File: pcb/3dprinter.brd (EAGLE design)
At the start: 100 x 80 mm, 79 parts, among them IC1 NRF51822, Q1 MOSFET, Q2 MOSFET, Q3 MOSFET, Q4 MOSFET, Y1 CRYSTAL

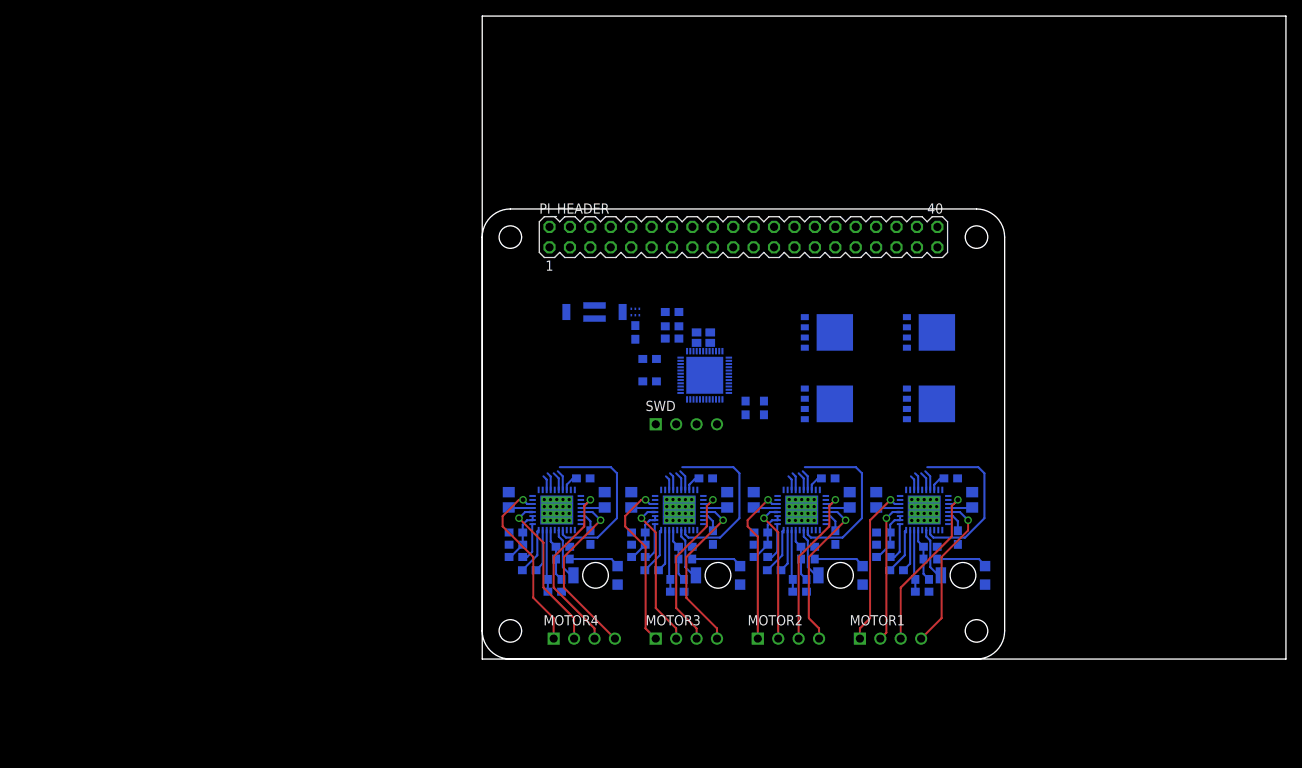
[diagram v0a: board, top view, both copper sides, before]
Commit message: Added regulator and fan mosfet
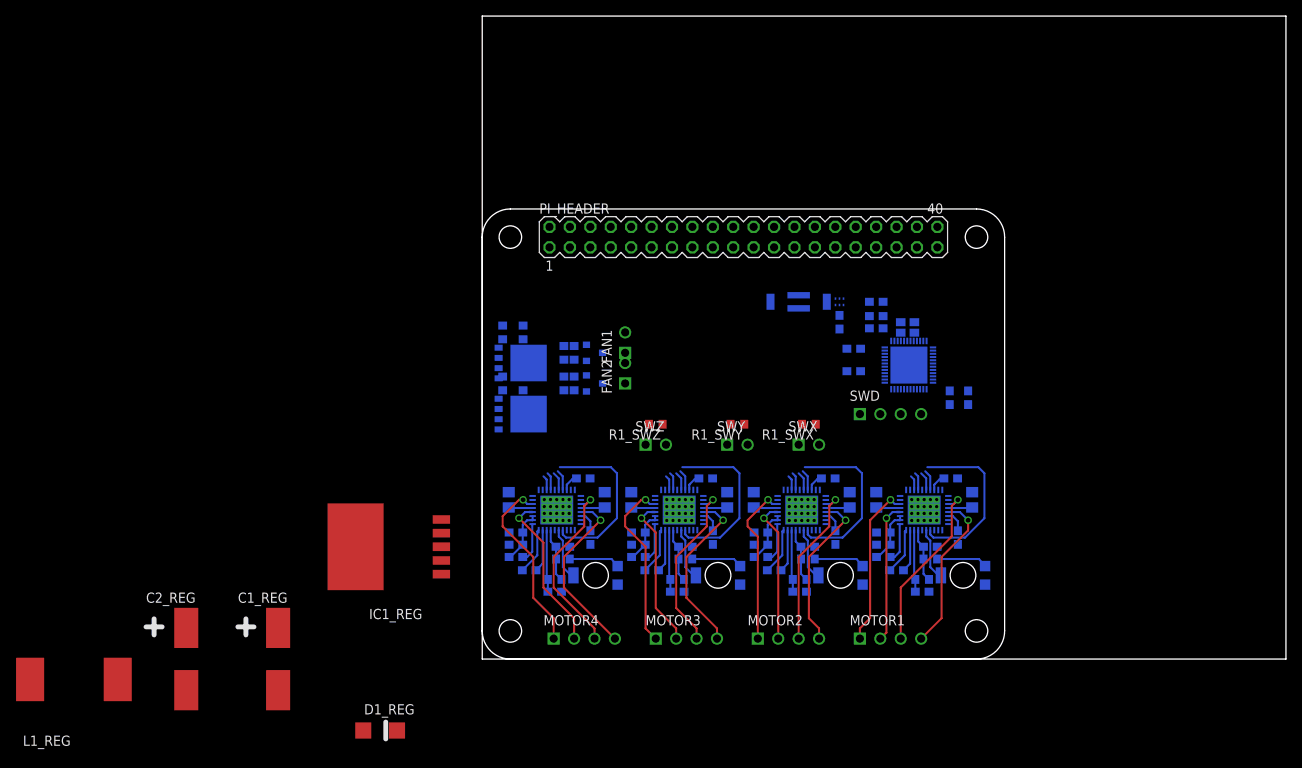
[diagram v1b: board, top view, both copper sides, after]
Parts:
- removed Q1, Q2, Q3, Q4: MOSFET, 3dprinter:MOSFET
- added C1_REG: 560u, 3dprinter:TANTULUM
- added C2_REG: 390u, 3dprinter:TANTULUM
- added D1_REG: SCHOTTKY, 3dprinter:SCHOTTKY
- added FAN1, FAN2, SWX, SWY, SWZ: (no value), 3dprinter:MA02-1
- added IC1_REG: REGULATOR, 3dprinter:REGULATOR
- added L1_REG: 33u, 3dprinter:INDUCTOR
- added Q1_BED, Q1_NOZ: MOSFET, 3dprinter:MOSFET
- added Q1_FAN1, Q1_FAN2: MOSFETSOT23, 3dprinter:SOT23
- added R1_BED, R1_FAN1, R1_FAN2, R1_NOZ: 100R, 3dprinter:R0603
- added R1_SWX, R1_SWY, R1_SWZ: 10k, 3dprinter:R0603
- added R2_BED, R2_FAN1, R2_FAN2, R2_NOZ: 100k, 3dprinter:R0603
- moved BAL 25.4 mm to (44.5, 44.5)
- moved C1 25.4 mm to (44.5, 41.9)
- moved C10 25.4 mm to (46.2, 35.8)
- moved C15 25.4 mm to (46.2, 38.6)
- moved Y1 25.4 mm to (52.9, 41.3)
- moved ANT 25.4 mm to (39.4, 44.5)
- moved C11 25.4 mm to (49.0, 41.1)
- moved C12 25.4 mm to (49.0, 44.5)
- moved C13 25.4 mm to (58.2, 32.5)
- moved C14 25.4 mm to (60.5, 32.5)
- moved C9 25.4 mm to (49.0, 42.7)
- moved IC1 25.4 mm to (53.1, 36.6)
- moved SWD 25.4 mm to (50.8, 30.5)
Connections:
- new net BED: R1_BED.1
- new net BEDG: Q1_BED.4, R1_BED.2, R2_BED.2
- new net FAN1: R1_FAN1.1
- new net FAN1-: FAN1.1, Q1_FAN1.3
- new net FAN1G: Q1_FAN1.1, R1_FAN1.2, R2_FAN1.2
- new net FAN2: R1_FAN2.1
- new net FAN2-: FAN2.1, Q1_FAN2.3
- new net FAN2G: Q1_FAN2.1, R1_FAN2.2, R2_FAN2.2
- new net N$11: Q1_NOZ.TAB
- new net N$12: Q1_BED.TAB
- new net N$13: D1_REG.C, IC1_REG.2, L1_REG.1
- new net NOZ: R1_NOZ.1
- new net NOZG: Q1_NOZ.4, R1_NOZ.2, R2_NOZ.2
- new net SWX: R1_SWX.1, SWX.2
- new net SWY: R1_SWY.1, SWY.2
- new net SWZ: R1_SWZ.1, SWZ.2
- net +12V: now also C1_REG.+, FAN1.2, FAN2.2, IC1_REG.1
- net +3V3: now also R1_SWX.2, R1_SWY.2, R1_SWZ.2
- net +5V: now also C2_REG.+, IC1_REG.4, L1_REG.2
- net GND: now also C1_REG.-, C2_REG.-, D1_REG.A, IC1_REG.3, IC1_REG.5, IC1_REG.TAB, Q1_BED.1, Q1_BED.2, Q1_BED.3, Q1_FAN1.2, Q1_FAN2.2, Q1_NOZ.1, Q1_NOZ.2, Q1_NOZ.3, R2_BED.1, R2_FAN1.1, R2_FAN2.1, R2_NOZ.1, SWX.1, SWY.1, SWZ.1

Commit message: Started component placment
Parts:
- added +12V: (no value), 3dprinter:MA04-1_5MM
- added BED, NOZ: (no value), 3dprinter:MA04-1
- added C3_REG: 1u, 3dprinter:C0805
- added C4_REG: 10n, 3dprinter:C0603
- added C5_REG: 2.2u, 3dprinter:C0805
- added IC2_REG: LP2985-3V3, 3dprinter:SOT23
- Q1_FAN1, Q1_FAN2: device 3dprinter:SOT23 -> 3dprinter:SOT23_FAN
- moved L1_REG 110.0 mm to (40.3, 59.1), flipped to the bottom, turned to 90 degrees
- moved C2_REG 97.4 mm to (37.0, 63.5)
- moved D1_REG 91.8 mm to (43.7, 63.6), flipped to the bottom
- moved C1_REG 89.4 mm to (37.5, 63.5), turned to 180 degrees
- moved IC1_REG 67.1 mm to (39.0, 64.5), flipped to the bottom
- moved R1_FAN1 49.2 mm to (48.0, 71.0), turned to 0 degrees
- moved R2_FAN1 43.8 mm to (36.0, 73.5), turned to 180 degrees
- moved Q1_FAN1 42.5 mm to (39.0, 72.5), turned to 180 degrees
- moved Q1_FAN2 40.1 mm to (29.0, 71.5), turned to 180 degrees
- moved R1_FAN2 37.5 mm to (25.5, 69.0), turned to 0 degrees
- moved R2_FAN2 34.7 mm to (23.0, 66.5), turned to 180 degrees
- moved FAN1 31.9 mm to (38.9, 64.6), turned to 270 degrees
- moved FAN2 30.6 mm to (30.4, 64.7), turned to 270 degrees
- moved ANT 19.7 mm to (59.0, 46.5), turned to 0 degrees
- moved SWZ 19.1 mm to (41.9, 24.9)
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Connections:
- net N$1 renamed IC1_XC2
- net N$10 renamed IC1_ANT2
- net N$13 renamed IC1_REG_OUT
- net N$2 renamed IC1_XC1
- net N$3 renamed IC1_DEC1
- net N$4 renamed IC1_DEC2
- net N$5 renamed PI_3V3
- net N$6 renamed IC1_AVDD
- net N$7 renamed ANT
- net N$8 renamed IC1_VDD_PA
- net N$9 renamed IC1_ANT1
- removed net N$11: Q1_NOZ.TAB
- removed net N$12: Q1_BED.TAB
- new net BED-: BED.1, BED.2, Q1_BED.TAB
- new net IC2_REG_BYPASS: C4_REG.1, IC2_REG.4
- new net NOZ-: NOZ.1, NOZ.2, Q1_NOZ.TAB
- net +12V: now also +12V.3, +12V.4, BED.3, BED.4, C3_REG.1, IC2_REG.1, IC2_REG.3, NOZ.3, NOZ.4
- net +3V3: now also C5_REG.1, IC2_REG.5
- net GND: now also +12V.1, +12V.2, C3_REG.2, C4_REG.2, C5_REG.2, IC2_REG.2
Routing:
- net OB1_M4: track 22.7 -> 0.00 mm, vias 1 -> 0
- net OA1_M4: track 22.7 -> 0.00 mm, vias 1 -> 0
- net OB2_M4: track 22.1 -> 0.00 mm, vias 1 -> 0
- net OB1_M3: track 21.6 -> 0.00 mm, vias 1 -> 0
- net OB1_M1: track 21.6 -> 0.00 mm, vias 1 -> 0
- net OA1_M3: track 21.6 -> 0.00 mm, vias 1 -> 0
- net OB2_M3: track 21.1 -> 0.00 mm, vias 1 -> 0
- net OB1_M2: track 20.6 -> 0.00 mm, vias 1 -> 0
- net OA1_M2: track 20.3 -> 0.00 mm, vias 1 -> 0
- net OA1_M1: track 20.3 -> 0.00 mm, vias 1 -> 0
- net OB2_M2: track 20.0 -> 0.00 mm, vias 1 -> 0
- net OB2_M1: track 20.0 -> 0.00 mm, vias 1 -> 0
- net OA2_M4: track 20.3 -> 0.42 mm, vias 1 -> 0
- net OA2_M3: track 19.2 -> 0.43 mm, vias 1 -> 0
- net OA2_M2: track 18.2 -> 0.42 mm, vias 1 -> 0
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
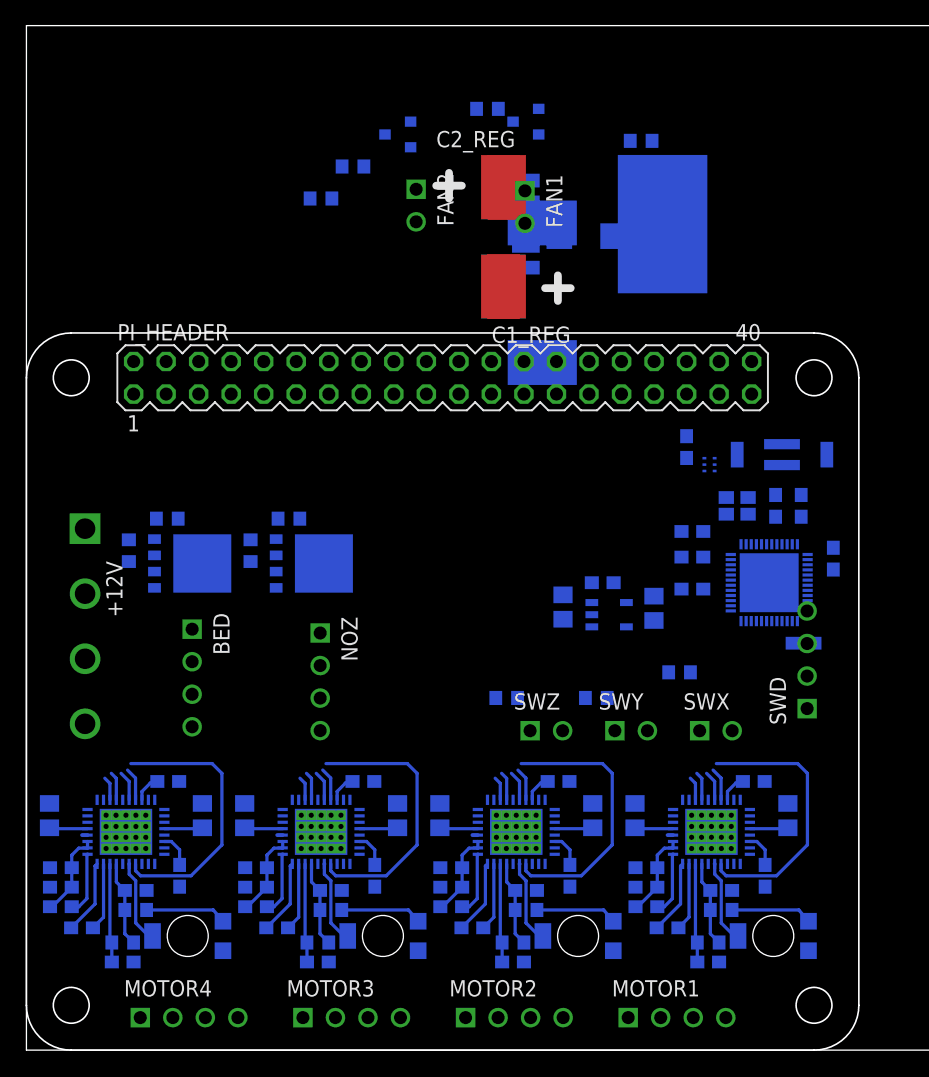
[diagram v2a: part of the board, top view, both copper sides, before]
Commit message: Rough component placement and started routing
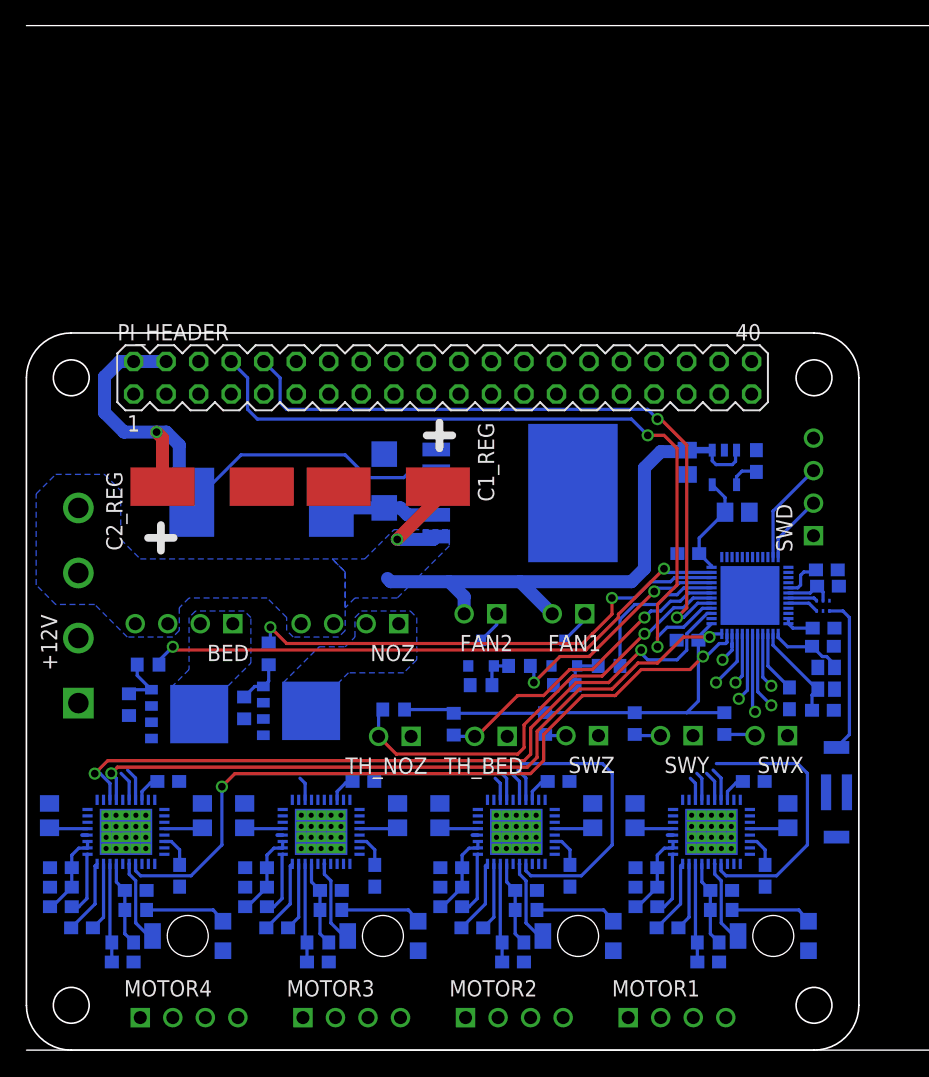
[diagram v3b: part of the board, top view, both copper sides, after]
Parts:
- added R3_BED, R3_NOZ: 100k, 3dprinter:R0603
- added TH_BED, TH_NOZ: (no value), 3dprinter:MA02-1
- moved R2_FAN1 45.4 mm to (42.0, 28.5)
- moved Q1_FAN1 41.6 mm to (42.0, 31.0), turned to 270 degrees
- moved R1_FAN2 41.1 mm to (38.5, 30.0)
- moved R1_FAN1 41.1 mm to (45.5, 30.0)
- moved Q1_FAN2 41.0 mm to (35.5, 31.0), turned to 270 degrees
- moved R2_FAN2 40.0 mm to (35.5, 28.5)
- moved FAN2 30.8 mm to (34.2, 34.1), turned to 180 degrees
- moved FAN1 30.6 mm to (41.1, 34.1), turned to 180 degrees
- moved C2_REG 29.8 mm to (14.5, 44.0), turned to 90 degrees
- moved L1_REG 27.4 mm to (18.4, 42.8), turned to 0 degrees
- moved ANT 26.7 mm to (63.3, 20.1), turned to 90 degrees
- moved D1_REG 24.8 mm to (27.9, 44.4), turned to 270 degrees
- moved IC1_REG 22.1 mm to (32.0, 43.5)
- moved C1_REG 21.6 mm to (28.3, 44.0), turned to 270 degrees
- moved C9 16.4 mm to (62.2, 26.5), turned to 180 degrees
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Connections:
- new net PI_3V32: PI_HEADER.17
- new net THBED: IC1.7, R3_BED.1, TH_BED.2
- new net THNOZ: IC1.6, R3_NOZ.1, TH_NOZ.2
- net +3V3: now also C6_M1.1, C6_M2.1, C6_M3.1, C6_M4.1, IC_M1.8, IC_M2.8, IC_M3.8, IC_M4.8, R3_BED.2, R3_NOZ.2
- net +5V: no longer C6_M1.1, C6_M2.1, C6_M3.1, C6_M4.1, IC_M1.8, IC_M2.8, IC_M3.8, IC_M4.8
- net BED: now also IC1.11
- net CFG1_M1: now also IC1.20
- net CFG1_M2: now also IC1.27
- net CFG1_M3: now also IC1.43
- net CFG1_M4: now also IC1.48
- net CFG2_M1: now also IC1.21
- net CFG2_M2: now also IC1.28
- net CFG2_M3: now also IC1.44
- net CFG2_M4: now also IC1.3
- net DIR_M1: now also IC1.18
- net DIR_M2: now also IC1.25
- net DIR_M3: now also IC1.41
- net DIR_M4: now also IC1.46
- net EN_M1: now also IC1.19
- net EN_M2: now also IC1.26
- net EN_M3: now also IC1.42
- net EN_M4: now also IC1.47
- net FAN1: now also IC1.8
- net FAN2: now also IC1.9
- net GND: now also TH_BED.1, TH_NOZ.1
- net IC1_ANT1: now also IC1.32; no longer IC1.31
- net IC1_ANT2: now also IC1.31; no longer IC1.32
- net NOZ: now also IC1.10
- net PI_14_TXD0: now also IC1.4
- net PI_15_RXD0: now also IC1.5
- net PI_3V3: no longer PI_HEADER.17
- net STEP_M1: now also IC1.17
- net STEP_M2: now also IC1.22
- net STEP_M3: now also IC1.40
- net STEP_M4: now also IC1.45
- net SWX: now also IC1.14
- net SWY: now also IC1.15
- net SWZ: now also IC1.16
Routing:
- net PI_14_TXD0: track 0.00 -> 61.1 mm, vias 0 -> 2
- net CFG2_M4: track 1.86 -> 58.9 mm, vias 0 -> 2
- net PI_15_RXD0: track 0.00 -> 53.8 mm, vias 0 -> 2
- net CFG1_M4: track 2.23 -> 55.6 mm, vias 0 -> 2
- net +12V: track 37.8 -> 91.0 mm, vias 0 -> 1
- net +3V3: track 0.00 -> 49.8 mm
- net BED: track 0.00 -> 46.9 mm, vias 0 -> 2
- net NOZ: track 0.00 -> 39.1 mm, vias 0 -> 2
- net EN_M4: track 21.5 -> 58.9 mm, vias 0 -> 2
- net +5V: track 8.72 -> 45.9 mm, vias 0 -> 1
- net THNOZ: track 0.00 -> 34.9 mm, vias 0 -> 1
- net THBED: track 0.00 -> 24.8 mm, vias 0 -> 1
- net FAN2: track 0.00 -> 18.5 mm, vias 0 -> 2
- net EN_M3: track 21.5 -> 6.17 mm, vias 0 -> 1
- net ANT: track 0.00 -> 12.3 mm
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- added copper zone on layer 16, net +12V
- added copper zone on layer 16, net BED-
- added copper zone on layer 16, net NOZ-

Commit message: More routing
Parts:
- moved R2_BED 4.17 mm to (8.51, 31.1), turned to 270 degrees
- moved C5_REG 3.61 mm to (51.9, 42.6), turned to 0 degrees
- moved C6_M1 3.54 mm to (60.1, 19.7)
- moved BED 2.41 mm to (14.6, 34.1)
- moved +12V 2.03 mm to (6.09, 34.7)
- moved R2_M1 1.63 mm to (60.7, 17.3)
- moved R1_NOZ 1.51 mm to (20.3, 31.5)
- moved NOZ 1.27 mm to (26.3, 34.1)
- moved C13 1.22 mm to (51.0, 39.8), turned to 90 degrees
- moved Q1_BED 1.10 mm to (9.40, 26.9)
- moved C10 1.00 mm to (63.5, 37.6), turned to 90 degrees
- moved R1_BED 0.97 mm to (9.91, 31.0), turned to 270 degrees
- moved C1 0.93 mm to (62.7, 35.3)
- moved R2_NOZ 0.80 mm to (16.3, 26.4)
- moved BAL 0.76 mm to (62.2, 33.9)
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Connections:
- net BED: now also IC1.7; no longer IC1.11
- net CFG1_M1: now also IC1.26; no longer IC1.20
- net CFG1_M2: now also IC1.18; no longer IC1.27
- net CFG1_M3: now also IC1.44; no longer IC1.43
- net CFG1_M4: now also IC1.5; no longer IC1.48
- net CFG2_M1: now also IC1.27; no longer IC1.21
- net CFG2_M2: now also IC1.17; no longer IC1.28
- net CFG2_M3: now also IC1.43; no longer IC1.44
- net CFG2_M4: now also IC1.6; no longer IC1.3
- net DIR_M1: now also IC1.22; no longer IC1.18
- net DIR_M2: now also IC1.20; no longer IC1.25
- net DIR_M3: now also IC1.46; no longer IC1.41
- net DIR_M4: now also IC1.3; no longer IC1.46
- net EN_M1: now also IC1.28; no longer IC1.19
- net EN_M2: now also IC1.21; no longer IC1.26
- net FAN1: now also IC1.14; no longer IC1.8
- net NOZ: now also IC1.8; no longer IC1.10
- net PI_14_TXD0: now also IC1.10; no longer IC1.4
- net PI_15_RXD0: now also IC1.11; no longer IC1.5
- net STEP_M1: now also IC1.25; no longer IC1.17
- net STEP_M2: now also IC1.19; no longer IC1.22
- net STEP_M3: now also IC1.45; no longer IC1.40
- net STEP_M4: now also IC1.4; no longer IC1.45
- net SWX: now also IC1.16; no longer IC1.14
- net SWY: now also IC1.41; no longer IC1.15
- net SWZ: now also IC1.40; no longer IC1.16
- net THBED: now also IC1.15; no longer IC1.7
- net THNOZ: now also IC1.48; no longer IC1.6
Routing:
- net CFG1_M2: track 2.23 -> 54.5 mm, vias 0 -> 2
- net DIR_M2: track 2.58 -> 54.3 mm, vias 0 -> 2
- net CFG2_M2: track 1.86 -> 52.2 mm, vias 0 -> 2
- net DIR_M4: track 5.18 -> 55.0 mm, vias 1 -> 2
- net STEP_M4: track 6.82 -> 56.0 mm, vias 1 -> 2
- net STEP_M2: track 2.33 -> 51.4 mm, vias 0 -> 2
- net CFG2_M3: track 5.87 -> 48.1 mm, vias 1 -> 2
- net STEP_M1: track 2.33 -> 44.3 mm, vias 0 -> 2
- net EN_M3: track 6.17 -> 46.9 mm, vias 1 -> 2
- net CFG1_M3: track 5.35 -> 45.3 mm, vias 1 -> 2
- net CFG2_M1: track 1.86 -> 41.6 mm, vias 0 -> 2
- net CFG1_M1: track 2.23 -> 40.9 mm, vias 0 -> 2
- net STEP_M3: track 4.33 -> 42.9 mm, vias 1 -> 2
- net DIR_M1: track 2.58 -> 41.1 mm, vias 0 -> 2
- net EN_M2: track 21.5 -> 57.8 mm, vias 0 -> 2
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- added copper zone on layer 1, net BED-
- added copper zone on layer 1, net GND
- added copper zone on layer 16, net GND
- added copper zone on layer 1, net NOZ-
